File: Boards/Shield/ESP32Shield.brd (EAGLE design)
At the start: 58.4 x 25.4 mm, 30 parts, among them Q1 220mA/50V/3.5Ω, U1 5V

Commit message: updating board
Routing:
- net ENC-B: track 0.00 -> 69.2 mm, vias 0 -> 1
- net ENC-A: track 0.00 -> 49.1 mm, vias 0 -> 2
- net CL: track 6.13 -> 14.3 mm
- net BTN: track 62.3 -> 64.1 mm
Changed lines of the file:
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@@
 <setting verticaltext="up"/>
 </settings>
-<grid distance="10" unitdist="mm" unit="mm" style="lines" multiple="1" display="yes" altdistance="0.005" altunitdist="inch" altunit="inch"/>
+<grid distance="0.05" unitdist="inch" unit="inch" style="lines" multiple="1" display="yes" altdistance="0.005" altunitdist="inch" altunit="inch"/>
 <layers>
 <layer number="1" name="Top" color="4" fill="1" visible="yes" active="yes"/>
@@
 <via x="26.67" y="17.78" extent="1-16" drill="0.381"/>
 <contactref element="S1" pad="C"/>
+<via x="10.16" y="-0.127" extent="1-16" drill="0.381"/>
+<wire x1="10.16" y1="-0.127" x2="3.81" y2="1.27" width="0" layer="19" extent="1-1"/>
+<via x="29.21" y="7.493" extent="1-16" drill="0.381"/>
+<via x="49.53" y="16.383" extent="1-16" drill="0.381"/>
+<via x="39.37" y="16.383" extent="1-16" drill="0.381"/>
 </signal>
 <signal name="BTN">
@@
 <via x="26.67" y="-1.27" extent="1-16" drill="0.381"/>
 <wire x1="26.67" y1="-1.27" x2="26.67" y2="0" width="0.2032" layer="16"/>
-<wire x1="26.67" y1="0" x2="25.4" y2="1.27" width="0.2032" layer="16"/>
-<wire x1="25.4" y1="1.27" x2="24.13" y2="1.27" width="0.2032" layer="16"/>
-<wire x1="24.13" y1="1.27" x2="22.86" y2="0" width="0.2032" layer="16"/>
-<wire x1="22.86" y1="0" x2="5.08" y2="0" width="0.2032" layer="16"/>
 <wire x1="26.67" y1="-1.27" x2="26.825" y2="-1.115" width="0.2032" layer="1"/>
 <contactref element="J6" pad="2"/>
@@
 <wire x1="39.205" y1="-0.165" x2="38.1" y2="-1.27" width="0.2032" layer="1"/>
 <wire x1="38.1" y1="-1.27" x2="26.67" y2="-1.27" width="0.2032" layer="1"/>
+<wire x1="5.08" y1="0" x2="6.985" y2="0" width="0.2032" layer="16"/>
+<wire x1="6.985" y1="0" x2="7.62" y2="0.635" width="0.2032" layer="16"/>
+<wire x1="7.62" y1="0.635" x2="7.62" y2="1.905" width="0.2032" layer="16"/>
+<wire x1="7.62" y1="1.905" x2="8.255" y2="2.54" width="0.2032" layer="16"/>
+<wire x1="8.255" y1="2.54" x2="24.13" y2="2.54" width="0.2032" layer="16"/>
+<wire x1="24.13" y1="2.54" x2="26.67" y2="0" width="0.2032" layer="16"/>
 </signal>
 <signal name="N$17">
@@
 <contactref element="LEFTEYE" pad="3"/>
 <wire x1="19.05" y1="1.27" x2="17.78" y2="0" width="0.2032" layer="1"/>
-<wire x1="17.78" y1="0" x2="15.24" y2="0" width="0.2032" layer="1"/>
+<wire x1="17.78" y1="0" x2="13.97" y2="0" width="0.2032" layer="1"/>
 <contactref element="J6" pad="6"/>
-<wire x1="13.97" y1="-1.27" x2="15.24" y2="0" width="0.2032" layer="1"/>
 <contactref element="RIGHTEYE" pad="3"/>
-<wire x1="8.89" y1="1.27" x2="13.97" y2="-1.27" width="0" layer="19" extent="1-1"/>
+<wire x1="13.97" y1="0" x2="13.335" y2="0" width="0.2032" layer="1"/>
+<wire x1="8.89" y1="1.27" x2="10.16" y2="2.54" width="0.2032" layer="1"/>
+<wire x1="10.16" y1="2.54" x2="12.065" y2="2.54" width="0.2032" layer="1"/>
+<wire x1="12.065" y1="2.54" x2="12.7" y2="1.905" width="0.2032" layer="1"/>
+<wire x1="12.7" y1="1.905" x2="12.7" y2="0.635" width="0.2032" layer="1"/>
+<wire x1="12.7" y1="0.635" x2="13.335" y2="0" width="0.2032" layer="1"/>
+<wire x1="13.97" y1="-1.27" x2="13.97" y2="0" width="0.2032" layer="1"/>
 </signal>
 <signal name="DR">
@@
 <contactref element="S1" pad="A"/>
 <contactref element="J6" pad="8"/>
-<wire x1="19.05" y1="-1.27" x2="52.07" y2="21.463" width="0" layer="19" extent="1-1"/>
+<wire x1="19.05" y1="-1.27" x2="20.32" y2="0" width="0.2032" layer="16"/>
+<wire x1="20.32" y1="0" x2="22.86" y2="0" width="0.2032" layer="16"/>
+<via x="22.86" y="0" extent="1-16" drill="0.381"/>
+<wire x1="22.86" y1="0" x2="38.1" y2="0" width="0.2032" layer="1"/>
+<wire x1="38.1" y1="0" x2="40.64" y2="2.54" width="0.2032" layer="1"/>
+<wire x1="40.64" y1="2.54" x2="40.64" y2="7.62" width="0.2032" layer="1"/>
+<via x="40.64" y="7.62" extent="1-16" drill="0.381"/>
+<wire x1="40.64" y1="7.62" x2="40.64" y2="8.89" width="0.2032" layer="16"/>
+<wire x1="40.64" y1="8.89" x2="41.91" y2="10.16" width="0.2032" layer="16"/>
+<wire x1="41.91" y1="10.16" x2="45.72" y2="10.16" width="0.2032" layer="16"/>
+<wire x1="45.72" y1="10.16" x2="52.07" y2="16.51" width="0.2032" layer="16"/>
+<wire x1="52.07" y1="16.51" x2="52.07" y2="21.463" width="0.2032" layer="16"/>
 </signal>
 <signal name="ENC-B">
 <contactref element="S1" pad="B"/>
 <contactref element="J6" pad="4"/>
-<wire x1="8.89" y1="-1.27" x2="46.99" y2="21.463" width="0" layer="19" extent="1-1"/>
+<wire x1="8.89" y1="-1.27" x2="7.62" y2="0" width="0.2032" layer="1"/>
+<wire x1="7.62" y1="0" x2="2.54" y2="0" width="0.2032" layer="1"/>
+<wire x1="2.54" y1="0" x2="1.905" y2="0.635" width="0.2032" layer="1"/>
+<wire x1="1.905" y1="0.635" x2="1.905" y2="3.81" width="0.2032" layer="1"/>
+<wire x1="1.905" y1="3.81" x2="2.54" y2="4.445" width="0.2032" layer="1"/>
+<wire x1="2.54" y1="4.445" x2="5.08" y2="4.445" width="0.2032" layer="1"/>
+<wire x1="5.08" y1="4.445" x2="6.35" y2="5.715" width="0.2032" layer="1"/>
+<via x="6.35" y="5.715" extent="1-16" drill="0.381"/>
+<wire x1="6.35" y1="5.715" x2="37.465" y2="5.715" width="0.2032" layer="16"/>
+<wire x1="37.465" y1="5.715" x2="39.37" y2="7.62" width="0.2032" layer="16"/>
+<wire x1="39.37" y1="7.62" x2="39.37" y2="10.16" width="0.2032" layer="16"/>
+<wire x1="39.37" y1="10.16" x2="40.64" y2="11.43" width="0.2032" layer="16"/>
+<wire x1="40.64" y1="11.43" x2="44.45" y2="11.43" width="0.2032" layer="16"/>
+<wire x1="44.45" y1="11.43" x2="46.99" y2="13.97" width="0.2032" layer="16"/>
+<wire x1="46.99" y1="13.97" x2="46.99" y2="21.463" width="0.2032" layer="16"/>
 </signal>
 <signal name="N$1">
@@
 <wire x1="11.43" y1="11.43" x2="11.938" y2="11.43" width="0.2032" layer="1"/>
 <wire x1="11.938" y1="11.43" x2="12.335" y2="11.827" width="0.2032" layer="1"/>
-<wire x1="12.335" y1="11.827" x2="12.335" y2="12.38" width="0" layer="19" extent="1-16"/>
+<wire x1="12.335" y1="11.827" x2="12.335" y2="12.38" width="0" layer="19" extent="1-1"/>
 </signal>
 <signal name="N$6">

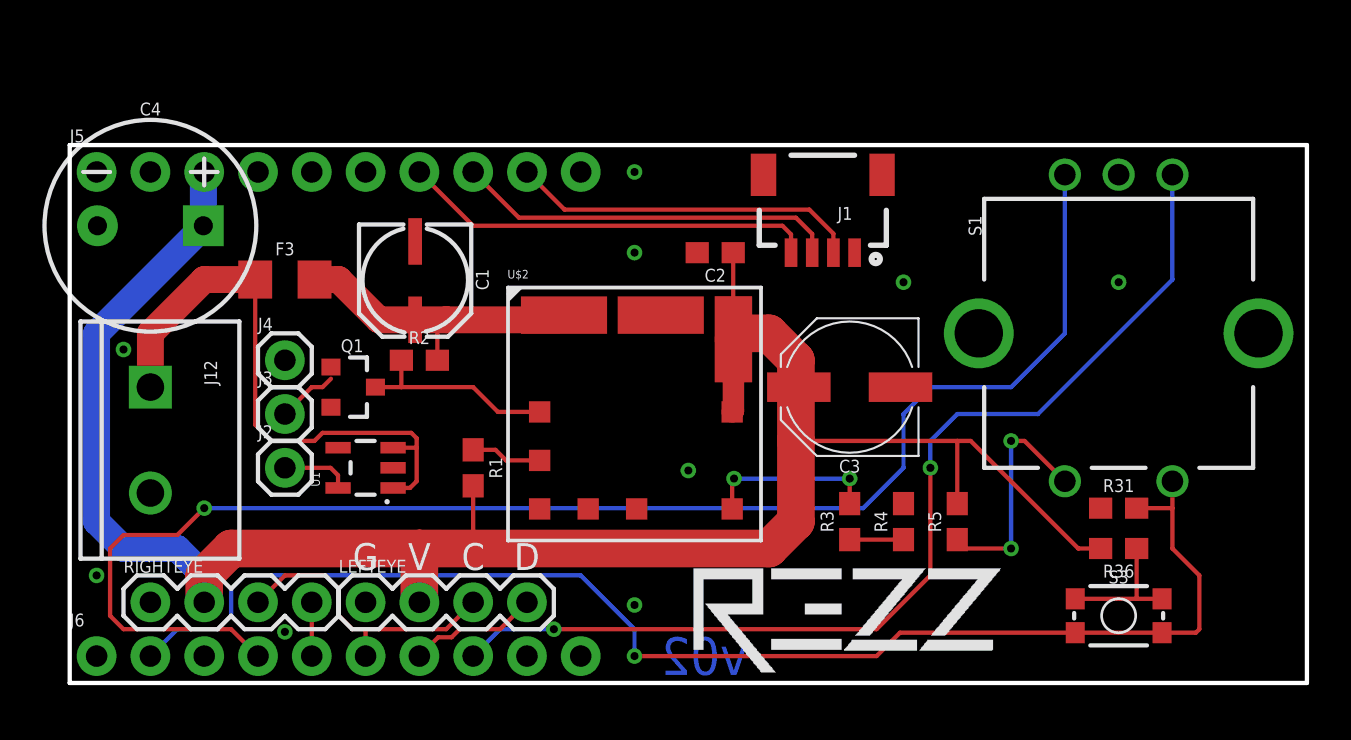
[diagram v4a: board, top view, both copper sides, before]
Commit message: adding new ESP8266Thing shield gerber
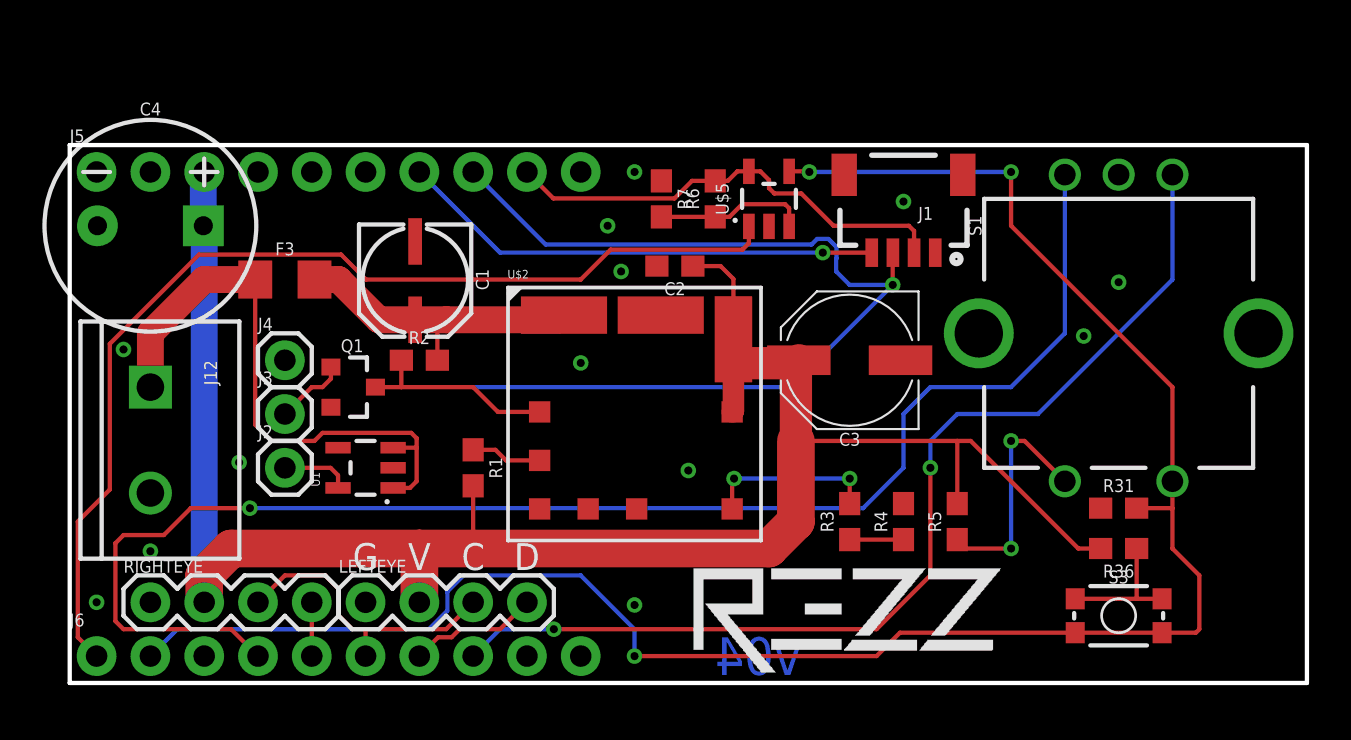
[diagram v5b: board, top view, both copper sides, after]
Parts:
- added R6: 100k, SparkFun-Resistors:0603
- added R7: 4.7k, SparkFun-Resistors:0603
- added U$5: OPA344, SparkFun-IC-Amplifiers:SOT23-5
- moved J1 3.81 mm to (39.4, 17.8)
- moved C2 2.01 mm to (28.6, 17.1)
- moved C3 1.27 mm to (36.8, 12.7)
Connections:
- new net N$9: R6.1, R7.2, U$5.3
- net 3.3V: now also R6.2, U$5.5
- net BTN: now also U$5.4
- net BTNINT: now also U$5.1
- net GND: now also R7.1, U$5.2
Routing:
- net BTNINT: track 0.00 -> 49.7 mm
- net SDA: track 18.1 -> 46.3 mm, vias 0 -> 1
- net BTN: track 64.1 -> 92.2 mm, vias 1 -> 3
- net N$9: track 0.00 -> 7.21 mm
- net 3.3V: track 16.6 -> 21.7 mm
- net 5V: track 100.1 -> 95.9 mm
- net SCL: track 19.6 -> 22.9 mm, vias 0 -> 1
- net N$1: track 2.87 -> 3.42 mm
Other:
- board text added: "v04"
- board text removed: "v02"

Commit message: Updating to ESP32 WROOM
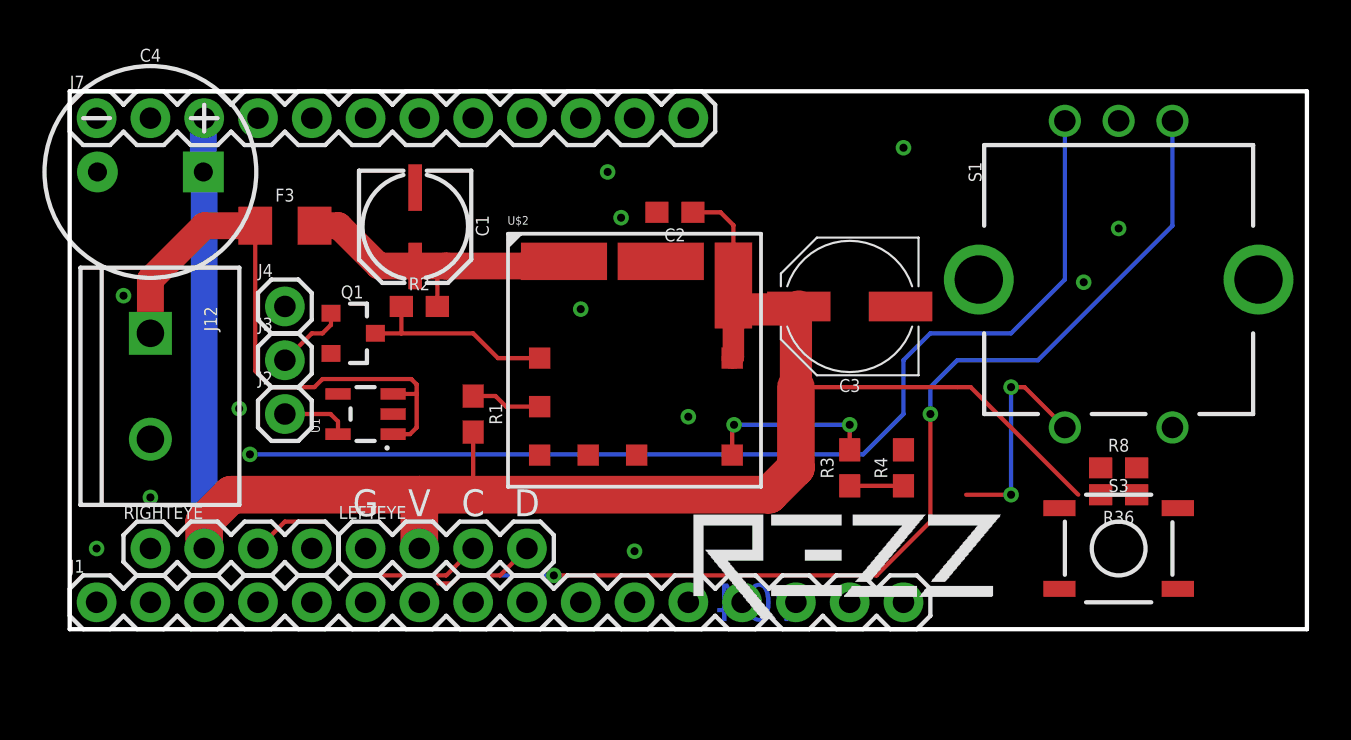
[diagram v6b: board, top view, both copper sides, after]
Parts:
- removed J5, J6: (no value), SparkFun-Connectors:1X10_NO_SILK
- removed R31: 10k, SparkFun-Resistors:0603
- removed R5: 43k, SparkFun-Resistors:0603
- removed R6: 100k, SparkFun-Resistors:0603
- removed R7: 4.7k, SparkFun-Resistors:0603
- removed U$5: OPA344, SparkFun-IC-Amplifiers:SOT23-5
- added J7: (no value), SparkFun-Connectors:1X12
- added R8: 100k, SparkFun-Resistors:0603
- J1: device SparkFun-Connectors:1X04_1MM_RA -> SparkFun-Connectors:1X16
- S3: value MOMENTARY-SWITCH-SPST-SMD-4.6X2.8MM -> MOMENTARY-SWITCH-SPST-SMD-5.2-REDUNDANT; device SparkFun-Switches:TACTILE_SWITCH_SMD_4.6X2.8MM -> SparkFun-Switches:TACTILE_SWITCH_SMD_5.2MM
- moved J1 41.5 mm to (1.27, 1.27), turned to 0 degrees
- moved S3 3.17 mm to (49.5, 3.81)
- moved C3 2.54 mm to (36.8, 15.2)
- moved J12 2.54 mm to (3.81, 14.0)
- moved J4 2.54 mm to (10.2, 15.2)
- moved Q1 2.54 mm to (13.3, 14.0)
- moved R2 2.54 mm to (16.5, 15.2)
- moved S1 2.54 mm to (49.5, 16.5)
- moved FRAME1 2.54 mm to (-2.54, -7.62)
- moved J2 2.54 mm to (10.2, 10.2)
- moved LEFTEYE 2.54 mm to (14.0, 3.81)
- moved R1 2.54 mm to (19.1, 10.2)
- moved R3 2.54 mm to (36.8, 7.62)
- moved R4 2.54 mm to (39.4, 7.62)
- moved RIGHTEYE 2.54 mm to (3.81, 3.81)
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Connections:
- removed net BTN: J6.2, R31.2, S1.SW-, S3.1, S3.2, U$5.4
- removed net BTNINT: J6.1, U$5.1
- removed net N$17: R36.1, S3.3, S3.4
- removed net N$6: R5.1, S1.SW+
- removed net N$9: R6.1, R7.2, U$5.3
- new net 13: J7.4
- new net 14: J7.10
- new net 15: J7.8
- new net 16: J1.14
- new net 17: J1.15
- new net 20: J7.5
- new net 23: J1.16
- new net 27: J7.6
- new net 32: J7.9
- new net 33: J7.7
- new net 3V3: J1.2
- new net A0: J1.5
- new net A1: J1.6
- new net A2: J1.7
- new net A3: J1.8
- new net A4: J1.9
- new net A5: J1.10
- new net BTN1: R36.2, S3.1, S3.2
- new net BTN2: R8.2, S1.SW-
- new net EN: J7.2
- new net MISO: J1.13
- new net MOSI: J1.12
- new net NC: J1.3
- new net RST: J1.1
- new net SCK: J1.11
- new net VBAT: J7.1
- new net VUSB: J7.3
- net 3.3V: now also S1.SW+, S3.3, S3.4; no longer J1.2, J5.9, R6.2, U$5.5
- net 5V: no longer J5.3, R36.2, R5.2
- net CL: no longer J6.6
- net DL: no longer J6.7
- net DR: no longer J6.5
- net ENC-A: no longer J6.8
- net ENC-B: no longer J6.4
- net GND: now also J1.4, R36.1, R8.1; no longer J1.1, J5.1, J5.10, J6.10, R31.1, R7.1, U$5.2
- net SCL: now also J7.11; no longer J1.4, J5.7
- net SDA: now also J7.12; no longer J1.3, J5.8
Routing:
- net BTN: track 92.2 -> 0.00 mm, vias 3 -> 0
- net BTNINT: track 49.7 -> 0.00 mm
- net SDA: track 46.3 -> 0.00 mm, vias 1 -> 0
- net SCL: track 22.9 -> 0.00 mm, vias 1 -> 0
- net ENC-B: track 69.0 -> 50.9 mm
- net 3.3V: track 21.7 -> 10.5 mm, vias 0 -> 2
- net N$6: track 11.1 -> 0.00 mm, vias 2 -> 0
- net N$9: track 7.21 -> 0.00 mm
- net N$17: track 6.48 -> 0.00 mm
- net 5V: track 95.9 -> 91.8 mm
- net DR: track 2.54 -> 0.00 mm
- net ENC-A: track 49.1 -> 47.3 mm
- net CL: track 14.3 -> 13.0 mm
- net DL: track 6.13 -> 4.87 mm

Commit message: updating shield
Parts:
- J1: device SparkFun-Connectors:1X16 -> SparkFun-Connectors:1X16_NO_SILK
- J7: device SparkFun-Connectors:1X12 -> SparkFun-Connectors:1X12_NO_SILK
- LEFTEYE, RIGHTEYE: device SparkFun-Connectors:1X04 -> SparkFun-Connectors:1X04_NO_SILK
- moved RIGHTEYE 33.1 mm to (36.8, 6.35)
- moved LEFTEYE 22.9 mm to (36.8, 3.81)
- moved U$4 19.8 mm to (49.5, 20.5)
- moved U$1 15.4 mm to (21.5, 5.11)
- moved J1 5.08 mm to (6.35, 1.27)
- moved J7 5.08 mm to (6.35, 24.1)
- moved R8 3.81 mm to (53.3, 7.62), turned to 180 degrees
- moved R2 2.84 mm to (19.1, 14.0)
- moved R3 2.54 mm to (36.8, 10.2), turned to 270 degrees
- moved R4 2.54 mm to (39.4, 10.2), turned to 270 degrees
- moved U$2 1.27 mm to (26.7, 14.0)
- moved R36 1.27 mm to (49.5, 7.62)
- moved C2 1.27 mm to (28.6, 21.0)
- moved Q1 1.27 mm to (14.6, 14.0)
- moved U$3 1.27 mm to (49.4, 12.4)
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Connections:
- removed net 14: J7.10
- removed net 16: J1.14
- removed net 17: J1.15
- removed net 23: J1.16
- removed net 27: J7.6
- removed net 32: J7.9
- removed net 33: J7.7
- removed net BTN1: R36.2, S3.1, S3.2
- removed net BTN2: R8.2, S1.SW-
- removed net CL: LEFTEYE.3, RIGHTEYE.3
- removed net DL: LEFTEYE.4
- removed net DR: RIGHTEYE.4
- removed net ENC-A: S1.A
- removed net ENC-B: S1.B
- removed net VUSB: J7.3
- new net 14/ENC-B: J7.10, S1.B
- new net 16/CLOCK: J1.14, LEFTEYE.3, RIGHTEYE.3
- new net 17/DR: J1.15, LEFTEYE.4
- new net 23/DL: J1.16, RIGHTEYE.4
- new net 27/BTN1: J7.6, R36.2, S3.1, S3.2
- new net 32/ENC-A: J7.9, S1.A
- new net 33/BTN2: J7.7, R8.2, S1.SW-
- net 5V: now also J7.3, LEFTEYE.1, RIGHTEYE.1; no longer LEFTEYE.2, RIGHTEYE.2
- net GND: now also LEFTEYE.2, RIGHTEYE.2; no longer LEFTEYE.1, RIGHTEYE.1
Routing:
- net 27/BTN1: track 0.00 -> 51.4 mm
- net ENC-B: track 50.9 -> 0.00 mm, vias 1 -> 0
- net ENC-A: track 47.3 -> 0.00 mm, vias 2 -> 0
- net 33/BTN2: track 0.00 -> 41.7 mm
- net 32/ENC-A: track 0.00 -> 26.4 mm
- net 5V: track 91.8 -> 72.3 mm, vias 0 -> 1
- net 14/ENC-B: track 0.00 -> 18.8 mm
- net CL: track 13.0 -> 0.00 mm
- net 3.3V: track 10.5 -> 23.0 mm, vias 2 -> 0
- net 16/CLOCK: track 0.00 -> 6.13 mm
- net 23/DL: track 0.00 -> 6.13 mm
- net DL: track 4.87 -> 0.00 mm
- net 17/DR: track 0.00 -> 3.59 mm
- net N$2: track 14.7 -> 16.4 mm
- net N$1: track 3.42 -> 5.03 mm
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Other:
- board text added: "+"
- board text added: "-"
- board text added: "B"
- board text added: "Y"
- board text added: "v05"
- board text removed: "C"
- board text removed: "D"
- board text removed: "G"
- board text removed: "V"
- board text removed: "v04"
